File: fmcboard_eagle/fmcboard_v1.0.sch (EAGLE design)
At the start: 39 parts, among them IC1 OPA699ID, IC2 OPA699ID, IC3 ICL7660CPA, IC4 ICL7660CPA, J1 8pin, J12 4p-2.54, J2 ASP-134604-01, J3 4p-2.54, J4 4p-2.54, J5 8pin, U1 TXS0108EPWR

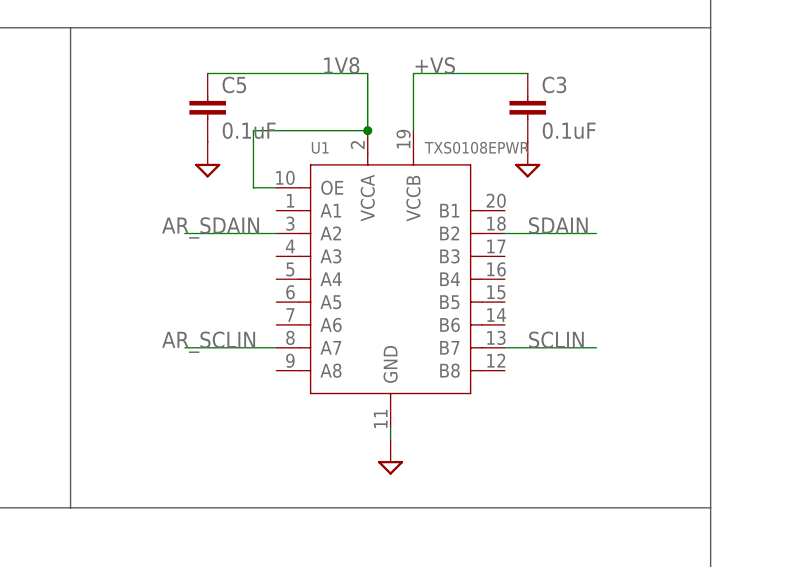
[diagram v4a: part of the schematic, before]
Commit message: switch sda scl 5v to 1.8
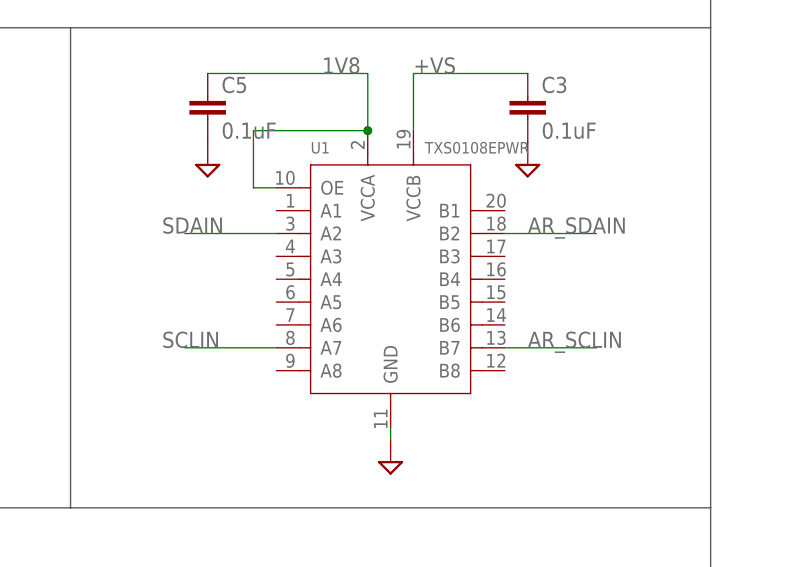
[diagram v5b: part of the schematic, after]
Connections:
- net AR_SCLIN: now also U1.B7; no longer U1.A7
- net AR_SDAIN: now also U1.B2; no longer U1.A2
- net SCLIN: now also U1.A7; no longer U1.B7
- net SDAIN: now also U1.A2; no longer U1.B2
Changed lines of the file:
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@@
 </segment>
 <segment>
-<pinref part="U1" gate="G$1" pin="B2"/>
-<wire x1="160.02" y1="86.36" x2="170.18" y2="86.36" width="0.1524" layer="91"/>
-<label x="162.56" y="86.36" size="1.778" layer="95"/>
+<pinref part="U1" gate="G$1" pin="A2"/>
+<wire x1="134.62" y1="86.36" x2="124.46" y2="86.36" width="0.1524" layer="91"/>
+<label x="121.92" y="86.36" size="1.778" layer="95"/>
 </segment>
 </net>
@@
 </segment>
 <segment>
+<pinref part="U1" gate="G$1" pin="A7"/>
+<wire x1="134.62" y1="73.66" x2="124.46" y2="73.66" width="0.1524" layer="91"/>
+<label x="121.92" y="73.66" size="1.778" layer="95"/>
+</segment>
+</net>
+<net name="AR_SDAIN" class="0">
+<segment>
+<pinref part="J5" gate="G$1" pin="6"/>
+<wire x1="78.74" y1="76.2" x2="63.5" y2="76.2" width="0.1524" layer="91"/>
+<label x="63.5" y="76.2" size="1.778" layer="95"/>
+</segment>
+<segment>
+<wire x1="60.96" y1="-40.64" x2="68.58" y2="-40.64" width="0.1524" layer="91"/>
+<label x="66.04" y="-40.64" size="1.778" layer="95"/>
+<pinref part="ARDUINO_NANO1" gate="G$1" pin="D11"/>
+</segment>
+<segment>
+<pinref part="U1" gate="G$1" pin="B2"/>
+<wire x1="160.02" y1="86.36" x2="170.18" y2="86.36" width="0.1524" layer="91"/>
+<label x="162.56" y="86.36" size="1.778" layer="95"/>
+</segment>
+</net>
+<net name="AR_SCLIN" class="0">
+<segment>
+<pinref part="J5" gate="G$1" pin="7"/>
+<wire x1="78.74" y1="73.66" x2="63.5" y2="73.66" width="0.1524" layer="91"/>
+<label x="63.5" y="73.66" size="1.778" layer="95"/>
+</segment>
+<segment>
+<wire x1="60.96" y1="-45.72" x2="68.58" y2="-45.72" width="0.1524" layer="91"/>
+<label x="66.04" y="-45.72" size="1.778" layer="95"/>
+<pinref part="ARDUINO_NANO1" gate="G$1" pin="D9"/>
+</segment>
+<segment>
 <pinref part="U1" gate="G$1" pin="B7"/>
 <wire x1="160.02" y1="73.66" x2="170.18" y2="73.66" width="0.1524" layer="91"/>
@@
 </segment>
 </net>
-<net name="AR_SDAIN" class="0">
-<segment>
-<pinref part="U1" gate="G$1" pin="A2"/>
-<wire x1="134.62" y1="86.36" x2="124.46" y2="86.36" width="0.1524" layer="91"/>
-<label x="121.92" y="86.36" size="1.778" layer="95"/>
-</segment>
-<segment>
-<pinref part="J5" gate="G$1" pin="6"/>
-<wire x1="78.74" y1="76.2" x2="63.5" y2="76.2" width="0.1524" layer="91"/>
-<label x="63.5" y="76.2" size="1.778" layer="95"/>
-</segment>
-<segment>
-<wire x1="60.96" y1="-40.64" x2="68.58" y2="-40.64" width="0.1524" layer="91"/>
-<label x="66.04" y="-40.64" size="1.778" layer="95"/>
-<pinref part="ARDUINO_NANO1" gate="G$1" pin="D11"/>
-</segment>
-</net>
-<net name="AR_SCLIN" class="0">
-<segment>
-<pinref part="U1" gate="G$1" pin="A7"/>
-<wire x1="134.62" y1="73.66" x2="124.46" y2="73.66" width="0.1524" layer="91"/>
-<label x="121.92" y="73.66" size="1.778" layer="95"/>
-</segment>
-<segment>
-<pinref part="J5" gate="G$1" pin="7"/>
-<wire x1="78.74" y1="73.66" x2="63.5" y2="73.66" width="0.1524" layer="91"/>
-<label x="63.5" y="73.66" size="1.778" layer="95"/>
-</segment>
-<segment>
-<wire x1="60.96" y1="-45.72" x2="68.58" y2="-45.72" width="0.1524" layer="91"/>
-<label x="66.04" y="-45.72" size="1.778" layer="95"/>
-<pinref part="ARDUINO_NANO1" gate="G$1" pin="D9"/>
-</segment>
-</net>

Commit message: Board v1.1
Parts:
- removed OPOUT_H10: BU-SMB-V, con-coax:BU-SMB-V
- added IO_G2, IO_G3, IO_H4, IO_H5: BU-SMB-V, con-coax:BU-SMB-V
- added R10, R12: 150, rcl:R-US_R0805
- added R11, R9: 750, rcl:R-US_R0805
- added R13, R14: 10k, rcl:R-US_R0805
- added R15, R16: 50, SparkFun-Resistors:RESISTORAXIAL-0.3
- R1: value 750 -> 100k; device SparkFun-Resistors:RESISTORAXIAL-0.3 -> resistor:R-TRIMM3296W
- R3: value 10k -> 100k; device SparkFun-Resistors:RESISTORAXIAL-0.3 -> rcl:R-US_R0805
- R4: value 150 -> 50
- R5: value 10k -> 50
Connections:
- new net AR_G36: ARDUINO_NANO1.D6, U1.B4
- new net AR_G37: ARDUINO_NANO1.D5, U1.B5
- new net G2: IO_G2.1, J2.G2, R4.2, SV2.16
- new net G3: IO_G3.1, J2.G3, R5.2, SV2.17
- new net G36: J2.G36, U1.A4
- new net G37: J2.G37, U1.A5
- new net H4: IO_H4.1, J2.H4, R15.2, SV2.13
- new net H5: IO_H5.1, J2.H5, R16.2, SV2.14
- new net N$7: IC2.INVERTING_INPUT, R11.1, R12.2
- new net N$8: R1.S, R3.2
- net +VS: now also R1.E
- net -VS: now also R1.A
- net GND: now also IO_G2.2, IO_G3.2, IO_H4.2, IO_H5.2, R10.1, R12.1, R15.1, R16.1, R4.1, R5.1; no longer OPOUT_H10.2, R4.2, SV2.17
- net N$1: now also R13.1, R14.1; no longer R3.1, R5.1
- net N$3: now also R10.2, R9.1; no longer R1.2, R4.1
- net OFFSETIN1: now also R14.2, R3.1; no longer R5.2
- net OPBUF1: now also R11.2, R13.2; no longer IC2.INVERTING_INPUT, R3.2
- net OPOUT1_H10: now also R9.2; no longer OPOUT_H10.1, R1.1
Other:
- note added: "Arduino"
- moved on the sheet: ARDUINO_NANO1, C10, C11, C7, C8, C9, IC1, IC2, OPIN, R2, R3, R4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

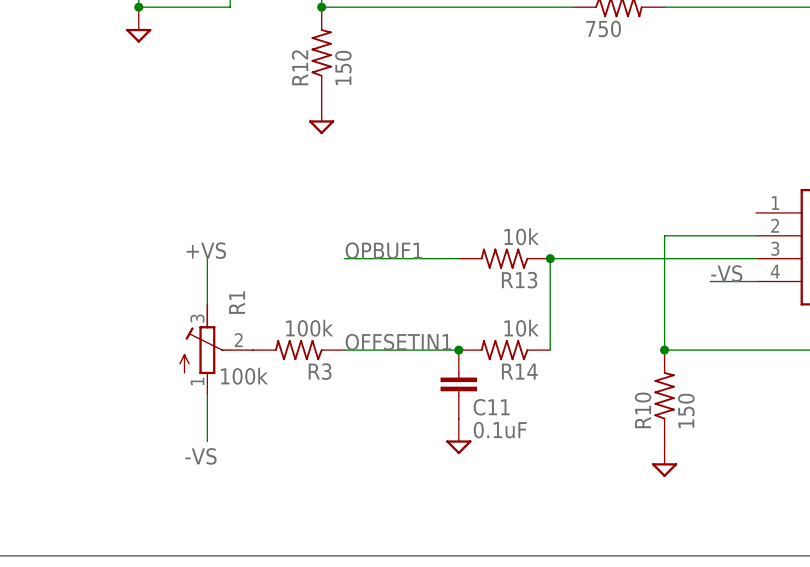
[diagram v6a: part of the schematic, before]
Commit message: Change resistors and labels
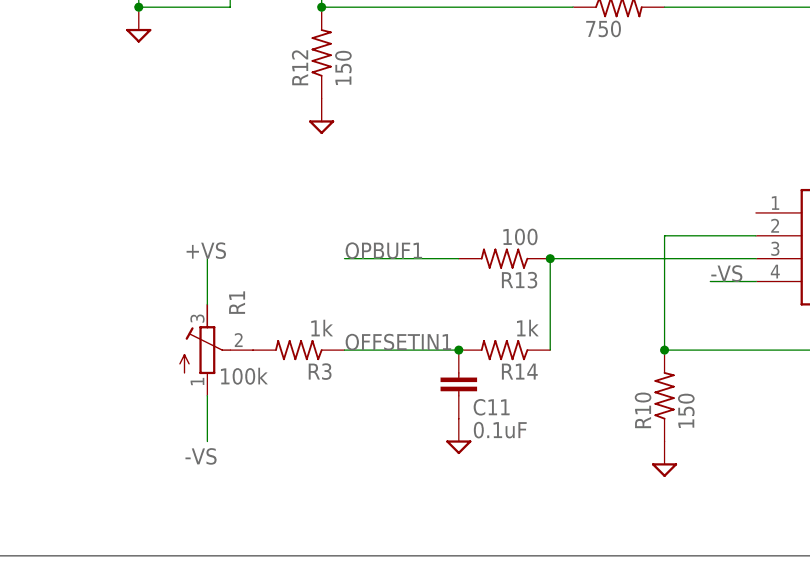
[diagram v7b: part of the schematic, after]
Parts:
- R13: value 10k -> 100
- R14: value 10k -> 1k
- R3: value 100k -> 1k
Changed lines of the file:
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@@
 <?xml version="1.0" encoding="utf-8"?>
 <!DOCTYPE eagle SYSTEM "eagle.dtd">
-<eagle version="9.5.2">
+<eagle version="9.6.2">
 <drawing>
 <settings>
@@
 <part name="R11" library="rcl" library_urn="urn:adsk.eagle:library:334" deviceset="R-US_" device="R0805" package3d_urn="urn:adsk.eagle:package:23553/2" value="750"/>
 <part name="R12" library="rcl" library_urn="urn:adsk.eagle:library:334" deviceset="R-US_" device="R0805" package3d_urn="urn:adsk.eagle:package:23553/2" value="150"/>
-<part name="R13" library="rcl" library_urn="urn:adsk.eagle:library:334" deviceset="R-US_" device="R0805" package3d_urn="urn:adsk.eagle:package:23553/2" value="10k"/>
-<part name="R14" library="rcl" library_urn="urn:adsk.eagle:library:334" deviceset="R-US_" device="R0805" package3d_urn="urn:adsk.eagle:package:23553/2" value="10k"/>
+<part name="R13" library="rcl" library_urn="urn:adsk.eagle:library:334" deviceset="R-US_" device="R0805" package3d_urn="urn:adsk.eagle:package:23553/2" value="100"/>
+<part name="R14" library="rcl" library_urn="urn:adsk.eagle:library:334" deviceset="R-US_" device="R0805" package3d_urn="urn:adsk.eagle:package:23553/2" value="1k"/>
 <part name="SUPPLY25" library="supply2" library_urn="urn:adsk.eagle:library:372" deviceset="GND" device=""/>
 <part name="R1" library="resistor" library_urn="urn:adsk.eagle:library:348" deviceset="R-TRIMM" device="3296W" package3d_urn="urn:adsk.eagle:package:26033/1" value="100k"/>
-<part name="R3" library="rcl" library_urn="urn:adsk.eagle:library:334" deviceset="R-US_" device="R0805" package3d_urn="urn:adsk.eagle:package:23553/2" value="100k"/>
+<part name="R3" library="rcl" library_urn="urn:adsk.eagle:library:334" deviceset="R-US_" device="R0805" package3d_urn="urn:adsk.eagle:package:23553/2" value="1k"/>
 <part name="IO_G2" library="con-coax" library_urn="urn:adsk.eagle:library:133" deviceset="BU-SMB-V" device="" package3d_urn="urn:adsk.eagle:package:6209/1"/>
 <part name="IO_G3" library="con-coax" library_urn="urn:adsk.eagle:library:133" deviceset="BU-SMB-V" device="" package3d_urn="urn:adsk.eagle:package:6209/1"/>

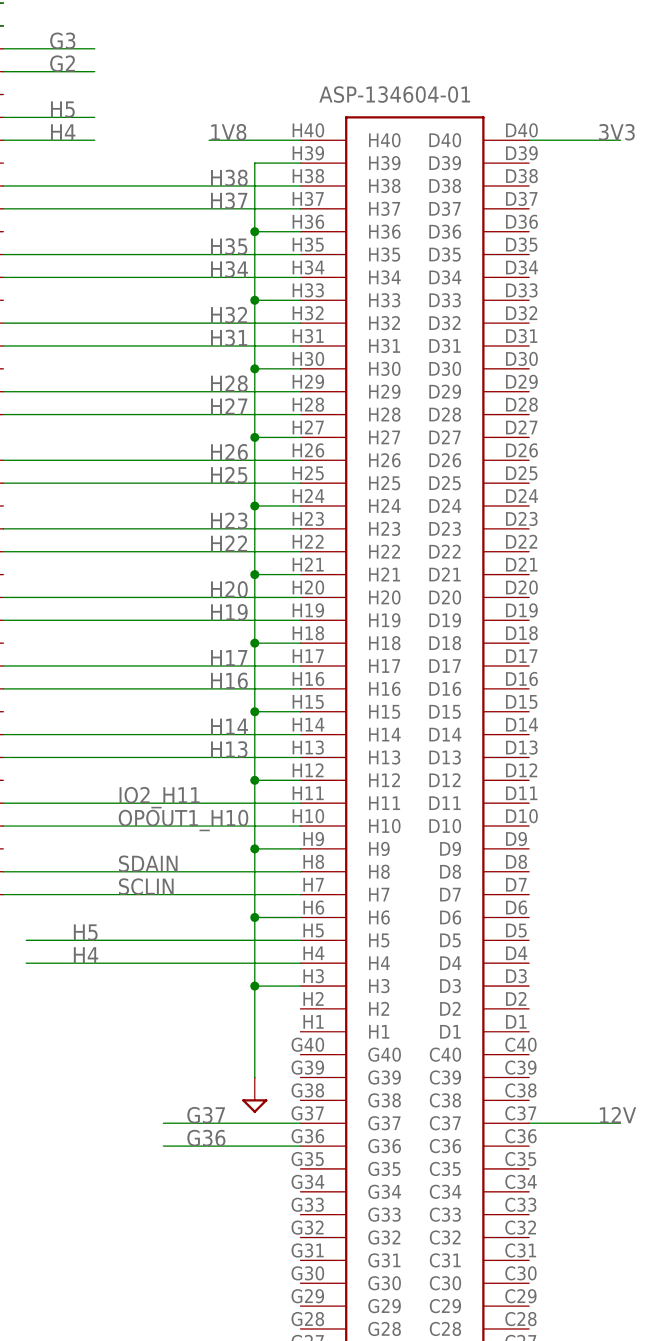
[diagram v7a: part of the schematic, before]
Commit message: Add more power connections to FMC header
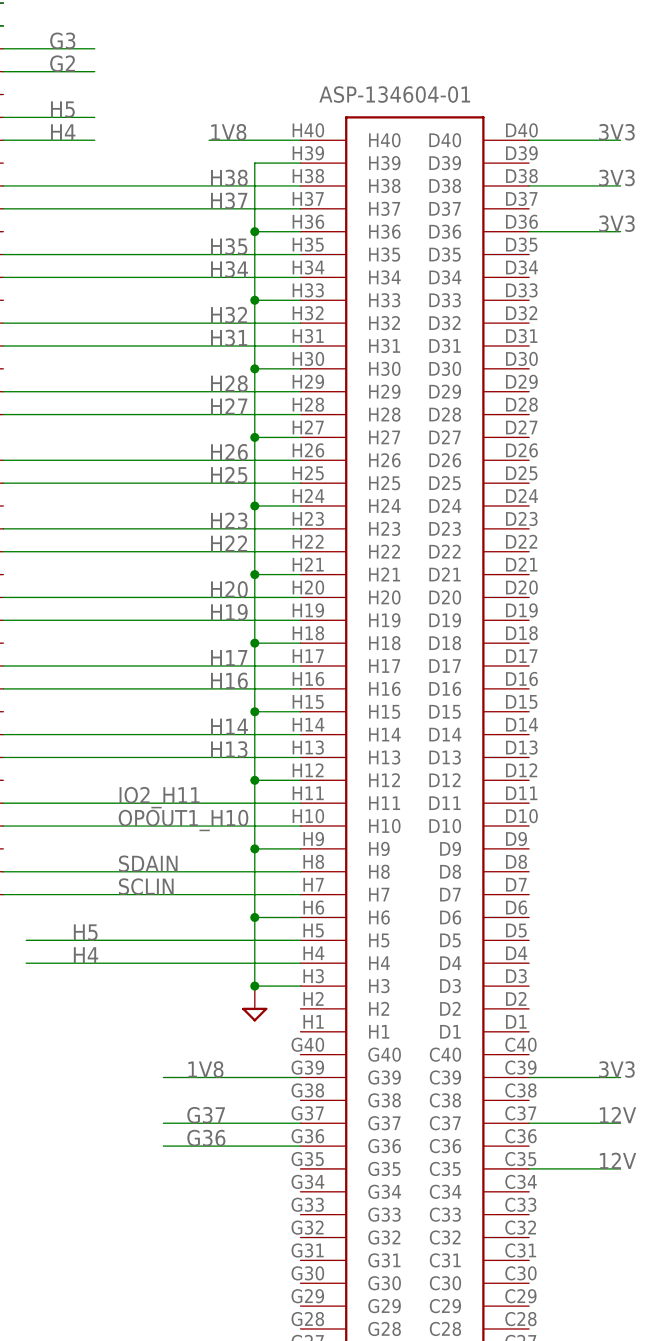
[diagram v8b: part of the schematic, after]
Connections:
- net 12V: now also J2.C35
- net 1V8: now also J2.G39
- net 3V3: now also J2.C39, J2.D36, J2.D38
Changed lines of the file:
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@@
 </instance>
 <instance part="SUPPLY1" gate="GND" x="81.28" y="119.38" smashed="yes"/>
-<instance part="SUPPLY2" gate="GND" x="248.92" y="81.28" smashed="yes"/>
+<instance part="SUPPLY2" gate="GND" x="248.92" y="91.44" smashed="yes"/>
 <instance part="J3" gate="G$1" x="154.94" y="1.27" smashed="yes"/>
 <instance part="J4" gate="G$1" x="139.7" y="1.27" smashed="yes"/>
@@
 </segment>
 <segment>
-<wire x1="248.92" y1="83.82" x2="248.92" y2="93.98" width="0.1524" layer="91"/>
 <pinref part="J2" gate="G$1" pin="H6"/>
 <wire x1="248.92" y1="93.98" x2="248.92" y2="101.6" width="0.1524" layer="91"/>
@@
 <label x="109.22" y="15.24" size="1.778" layer="95"/>
 </segment>
+<segment>
+<wire x1="254" y1="83.82" x2="238.76" y2="83.82" width="0.1524" layer="91"/>
+<pinref part="J2" gate="G$1" pin="G39"/>
+<label x="241.3" y="83.82" size="1.778" layer="95"/>
+</segment>
 </net>
 <net name="3V3" class="1">
@@
 <label x="101.6" y="15.24" size="1.778" layer="95"/>
 </segment>
+<segment>
+<pinref part="J2" gate="G$1" pin="C39"/>
+<wire x1="279.4" y1="83.82" x2="289.56" y2="83.82" width="0.1524" layer="91"/>
+<label x="287.02" y="83.82" size="1.778" layer="95"/>
+</segment>
+<segment>
+<wire x1="279.4" y1="182.88" x2="289.56" y2="182.88" width="0.1524" layer="91"/>
+<pinref part="J2" gate="G$1" pin="D38"/>
+<label x="287.02" y="182.88" size="1.778" layer="95"/>
+</segment>
+<segment>
+<wire x1="279.4" y1="177.8" x2="289.56" y2="177.8" width="0.1524" layer="91"/>
+<pinref part="J2" gate="G$1" pin="D36"/>
+<label x="287.02" y="177.8" size="1.778" layer="95"/>
+</segment>
 </net>
 <net name="12V" class="1">
@@
 <label x="93.98" y="15.24" size="1.778" layer="95"/>
 </segment>
+<segment>
+<wire x1="279.4" y1="73.66" x2="289.56" y2="73.66" width="0.1524" layer="91"/>
+<pinref part="J2" gate="G$1" pin="C35"/>
+<label x="287.02" y="73.66" size="1.778" layer="95"/>
+</segment>
 </net>
